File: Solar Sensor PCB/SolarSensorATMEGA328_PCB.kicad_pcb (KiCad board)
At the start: 2 copper layers, 44.9 x 44.9 mm, 33 parts, among them P1 I2C, P10 I2C, P2 SERIAL, P3 ID, P4 ISP, P5 LOGO2, P6 PCB, P8 ADC, P9 PROG, SW1 SWA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

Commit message: updated new PCB version
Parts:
- added C11: 100n, REInnovationFootprint:SM_C_0805, F.Cu at (170.8, 112.9)
- added J1: ANALOG, REInnovationFootprint:SIL-3_screw_terminal, F.Cu at (155.1, 115.7)
- added R2: 10k, REInnovationFootprint:SM0805, F.Cu at (170.1, 116.5)
- P6: footprint REInnovationFootprint:PCB_45_45_Cut_Out_Solar_Sensor -> REInnovationFootprint:PCB_SolarSensorATMEGA328_PCB_design_v2
- moved SW2 85.7 mm to (219.7, 123.6)
- moved R5 85.7 mm to (219.7, 117.1), turned to 0 degrees
- moved P9 79.1 mm to (205.7, 133.5), turned to 180 degrees
- moved P6 77.4 mm to (203.5, 136.1)
- moved C9 75.6 mm to (225.1, 104.8), turned to 0 degrees
- moved R4 68.5 mm to (227.8, 118.4)
- moved Y1 66.9 mm to (220.6, 101.0), turned to 180 degrees
- moved C3 63.4 mm to (198.8, 107.6), turned to 270 degrees
- moved C4 62.0 mm to (194.0, 96.5), turned to 180 degrees
- moved C10 61.6 mm to (211.5, 101.9), turned to 90 degrees
- moved SW1 60.6 mm to (224.3, 123.6)
- moved P3 59.6 mm to (226.1, 112.8), turned to 270 degrees
- moved D2 58.7 mm to (227.8, 125.4)
- moved C8 58.7 mm to (193.0, 123.8)
- moved P2 57.7 mm to (206.3, 124.8)
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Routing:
- net VCC: track 246.2 -> 12.7 mm, vias 7 -> 0
- net GND: track 227.1 -> 32.1 mm, vias 3 -> 0
- net /I2C_SDA: track 89.1 -> 0.00 mm, vias 3 -> 0
- net /I2C_CLK: track 79.6 -> 0.00 mm, vias 2 -> 0
- net /ATMega328/RESET: track 64.8 -> 0.00 mm, vias 3 -> 0
- net /Rx: track 57.4 -> 12.1 mm, vias 1 -> 0
- net /Tx: track 55.6 -> 16.5 mm, vias 1 -> 0
- net /ATMega328/MOSI: track 30.5 -> 0.00 mm, vias 2 -> 0
- net /ATMega328/MISO: track 29.1 -> 0.00 mm, vias 1 -> 0
- net /ATMega328/SCLK: track 25.0 -> 0.00 mm, vias 1 -> 0
- net Net-(C1-Pad2): track 17.4 -> 0.00 mm
- net /ATMega328/A2: track 13.5 -> 0.00 mm, vias 2 -> 0
- net Net-(C1-Pad1): track 13.2 -> 0.00 mm
- net /ATMega328/A1: track 13.2 -> 0.00 mm
- net Net-(D2-Pad2): track 11.7 -> 0.00 mm
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- removed copper zone on B.Cu, net GND
- removed copper zone on F.Cu, net GND
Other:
- board size 44.9 x 44.9 mm -> 51.2 x 45.6 mm

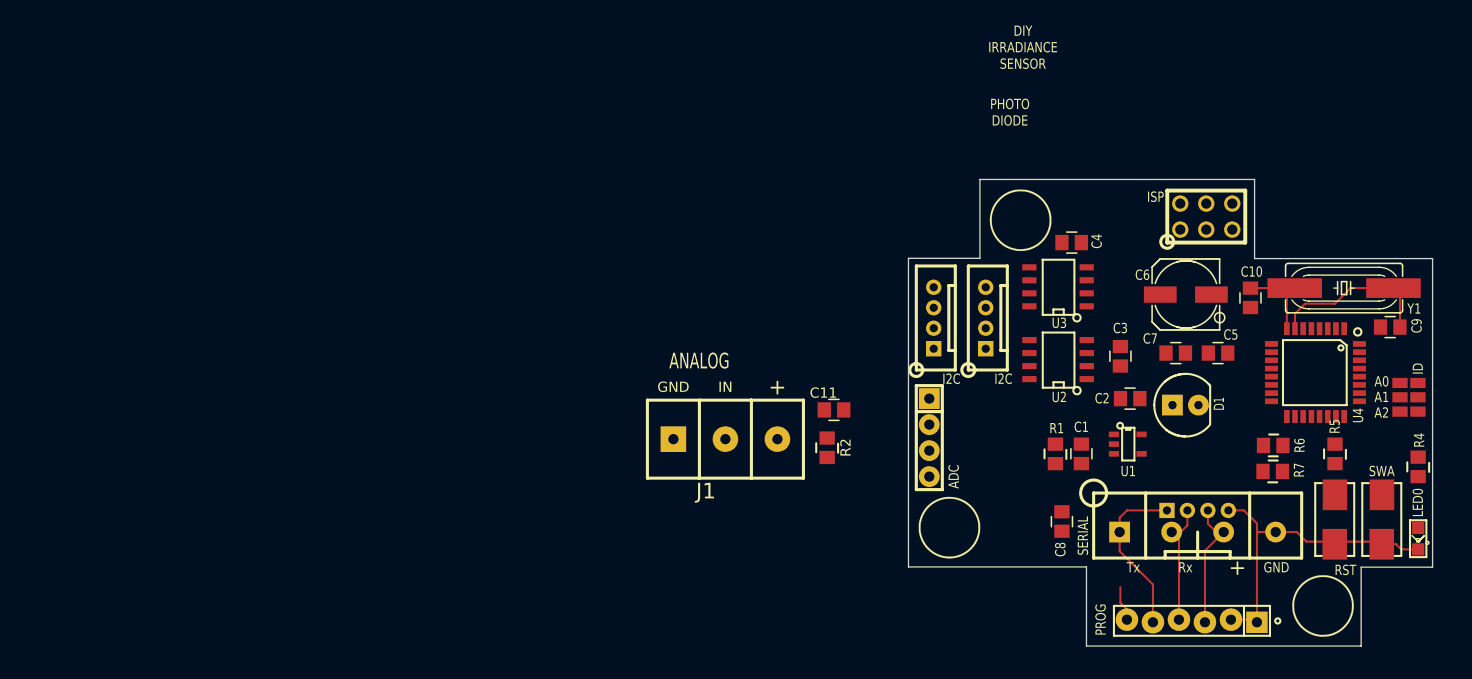
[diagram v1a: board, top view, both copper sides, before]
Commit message: Updated PCB and Firmware
Added 3D models to new Kicad PCB
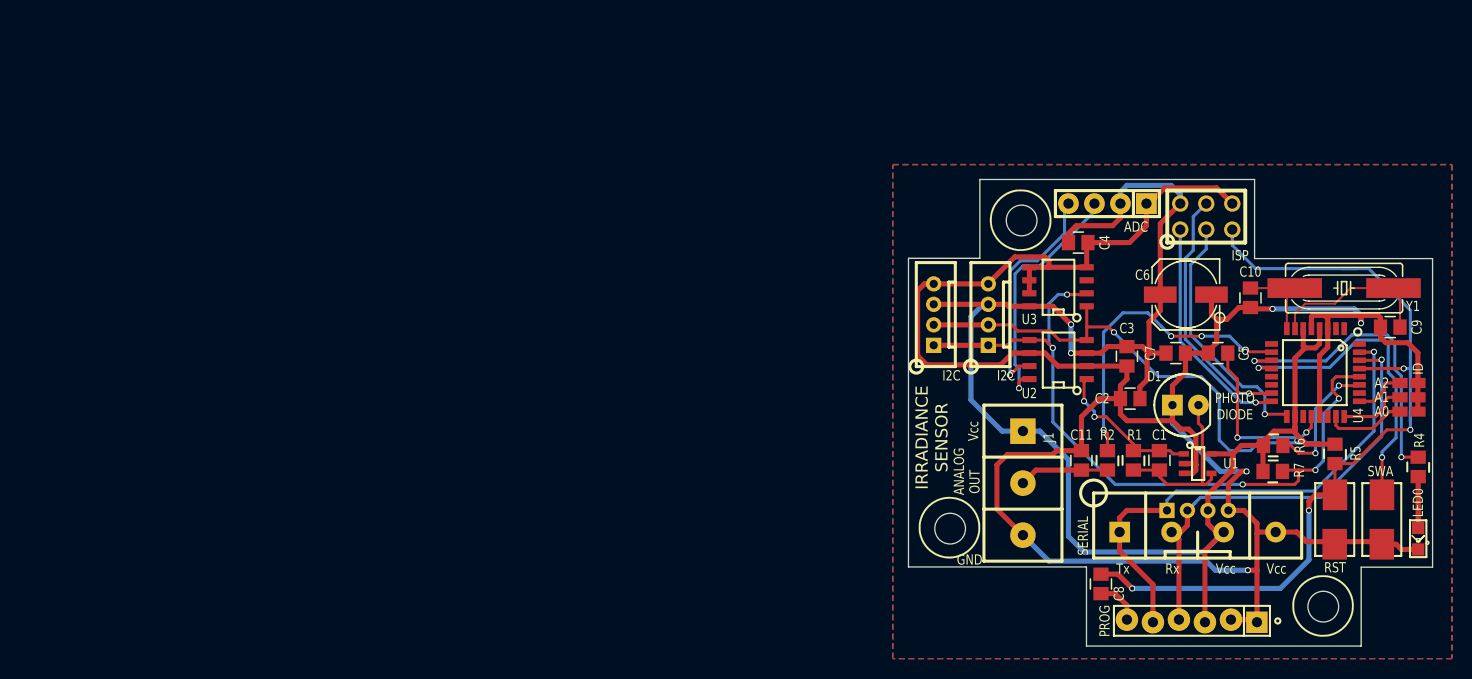
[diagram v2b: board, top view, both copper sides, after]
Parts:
- D1: footprint REInnovationFootprint:LED-5MM_larg_pad -> REInnovationFootprint:LED-5MM_PHOTODIODE
- moved P5 62.1 mm to (223.8, 106.3)
- moved J1 34.1 mm to (189.2, 114.9), turned to 270 degrees
- moved P8 28.7 mm to (197.5, 92.7), turned to 180 degrees
- moved R2 27.4 mm to (197.5, 117.8)
- moved C11 24.7 mm to (194.9, 117.8), turned to 90 degrees
- moved C1 7.65 mm to (202.6, 117.8)
- moved R1 7.65 mm to (200.0, 117.8)
- moved C8 7.19 mm to (196.8, 129.9)
- moved U1 7.09 mm to (204.9, 118.1)
- moved C4 0.64 mm to (194.6, 96.5)
- moved C3 0.63 mm to (199.4, 107.6)
- moved P1 0.42 mm to (188.0, 103.6)
- moved P10 0.33 mm to (182.6, 103.6)
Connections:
- P3 pad 1: /ATMega328/A0 -> /ATMega328/A2
- P3 pad 5: /ATMega328/A2 -> /ATMega328/A0
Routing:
- net GND: track 32.1 -> 251.0 mm, vias 0 -> 4
- net VCC: track 12.7 -> 160.5 mm, vias 0 -> 2
- net /ATMega328/RESET: track 0.00 -> 85.1 mm, vias 0 -> 4
- net /I2C_CLK: track 0.00 -> 71.7 mm, vias 0 -> 5
- net /I2C_SDA: track 0.00 -> 62.2 mm, vias 0 -> 3
- net /Tx: track 16.5 -> 49.7 mm, vias 0 -> 1
- net /Rx: track 12.1 -> 45.0 mm, vias 0 -> 1
- net /ATMega328/D6: track 0.00 -> 31.1 mm, vias 0 -> 4
- net /ATMega328/D8_SWA: track 0.00 -> 30.9 mm, vias 0 -> 2
- net /ATMega328/D7_LED0: track 0.00 -> 29.9 mm, vias 0 -> 2
- net /ATMega328/SCLK: track 0.00 -> 24.7 mm, vias 0 -> 1
- net /ATMega328/MOSI: track 0.00 -> 24.7 mm, vias 0 -> 1
- net Net-(P8-Pad3): track 0.00 -> 24.1 mm, vias 0 -> 1
- net Net-(P8-Pad4): track 0.00 -> 22.4 mm, vias 0 -> 1
- net /ATMega328/MISO: track 0.00 -> 22.4 mm, vias 0 -> 1
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- added copper zone on B.Cu, net GND
- added copper zone on F.Cu, net GND
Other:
- board text added: "IRRADIANCE SENSOR"
- board text added: "Vcc"
- board text removed: "+"
- board text removed: "GND"

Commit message: Updated firmware.
Sorted serial requests
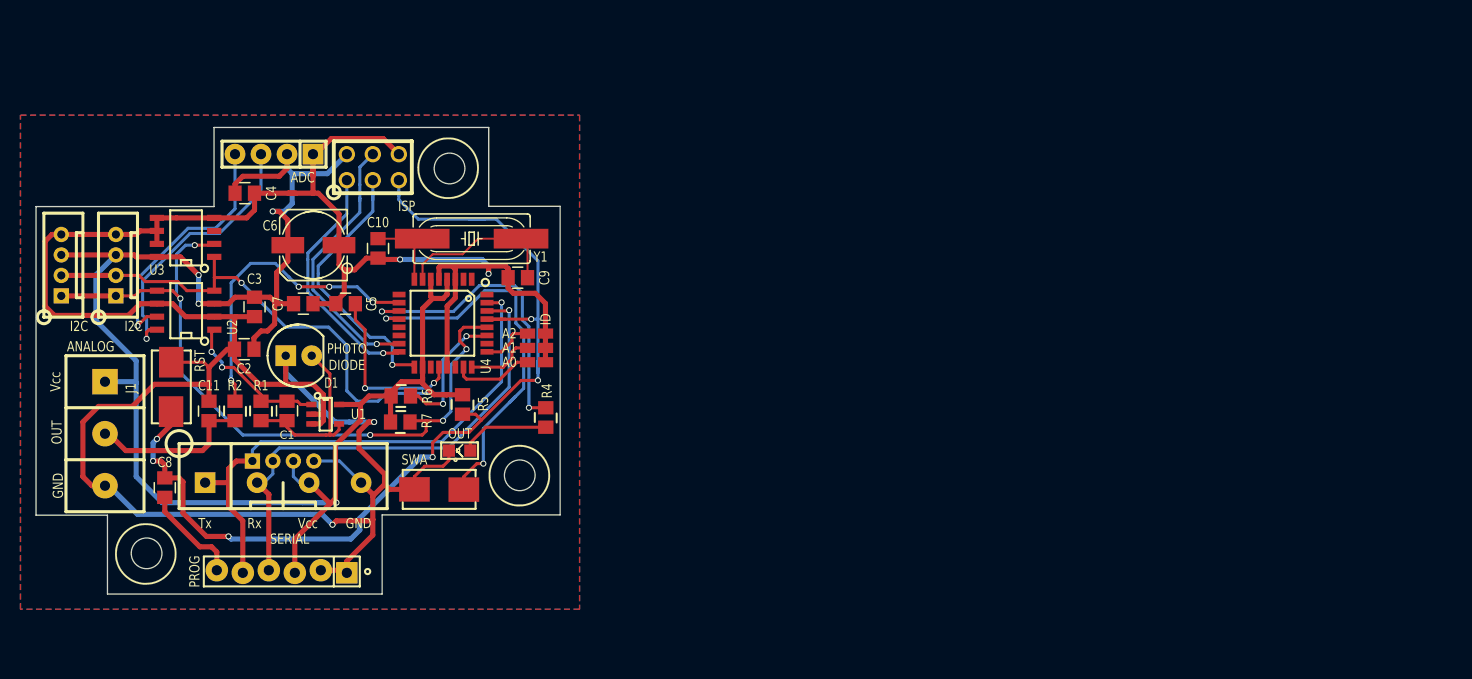
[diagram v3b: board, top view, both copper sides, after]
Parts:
- D2: value LED0 -> OUT
- moved SW2 114.4 mm to (106.0, 110.6), turned to 90 degrees
- moved D2 94.0 mm to (134.2, 116.8), turned to 90 degrees
- moved SW1 92.1 mm to (132.2, 120.6), turned to 180 degrees
- moved C8 91.9 mm to (105.4, 120.5)
- moved J1 89.8 mm to (99.6, 110.1)
- moved P2 89.5 mm to (117.0, 120.0)
- moved P9 89.0 mm to (116.8, 128.7)
- moved D1 86.7 mm to (118.5, 107.6)
- moved C2 86.7 mm to (113.2, 106.9)
- moved P6 85.4 mm to (118.2, 131.1)
- moved C10 85.4 mm to (126.2, 97.1)
- moved C6 85.4 mm to (119.9, 96.8)
- moved P1 85.4 mm to (102.7, 98.7)
- moved P3 85.4 mm to (140.8, 108.0)
- moved P5 85.4 mm to (138.6, 101.5)
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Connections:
- P6 pad 1: Net-(P6-Pad1) -> (no net)
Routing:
- net GND: track 251.0 -> 268.3 mm
- net /ATMega328/RESET: track 85.1 -> 98.8 mm, vias 4 -> 6
- net VCC: track 160.5 -> 173.2 mm, vias 2 -> 4
- net /ATMega328/D8_SWA: track 30.9 -> 38.3 mm
- net /IRR_A: track 8.78 -> 15.6 mm
- net /ATMega328/DTR: track 4.41 -> 9.89 mm
- net /Tx: track 49.7 -> 54.1 mm
- net Net-(D2-Pad2): track 5.01 -> 8.76 mm
- net /Rx: track 45.0 -> 48.3 mm
- net Net-(P8-Pad3): track 24.1 -> 27.2 mm
- net /ATMega328/SCLK: track 24.7 -> 26.9 mm
- net Net-(P8-Pad4): track 22.4 -> 24.6 mm
- net /ATMega328/MOSI: track 24.7 -> 26.6 mm
- net /ATMega328/MISO: track 22.4 -> 23.9 mm
- net Net-(C1-Pad2): track 17.3 -> 17.8 mm
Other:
- outline, holes or cut-outs redrawn
- board text added: "GND"
- board text removed: "IRRADIANCE SENSOR"

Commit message: Large update
Add CRC to firmware
Update readme
Update PCB to kicad 9
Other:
- net class Default removed
